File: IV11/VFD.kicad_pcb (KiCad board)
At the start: 2 copper layers, 225 x 80 mm, 72 parts, among them J1 USB_B, J2 I2C_CONN, SW1 switch, SW2 switch, SW3 switch, SW4 switch, U1 74HC595, U10 UDN2981, U11 UDN2981, U12 UDN2981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

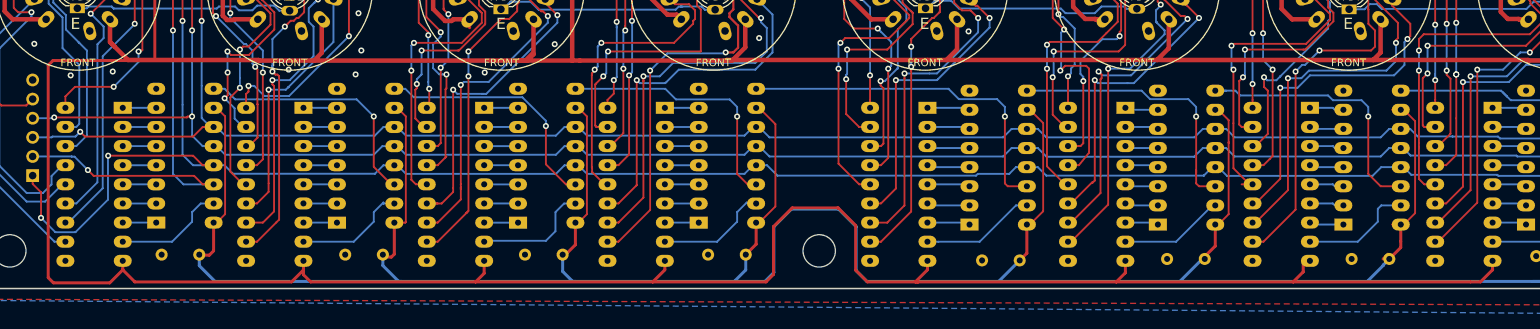
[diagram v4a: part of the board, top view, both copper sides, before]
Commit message: Update thickness of 48VDC tracks x
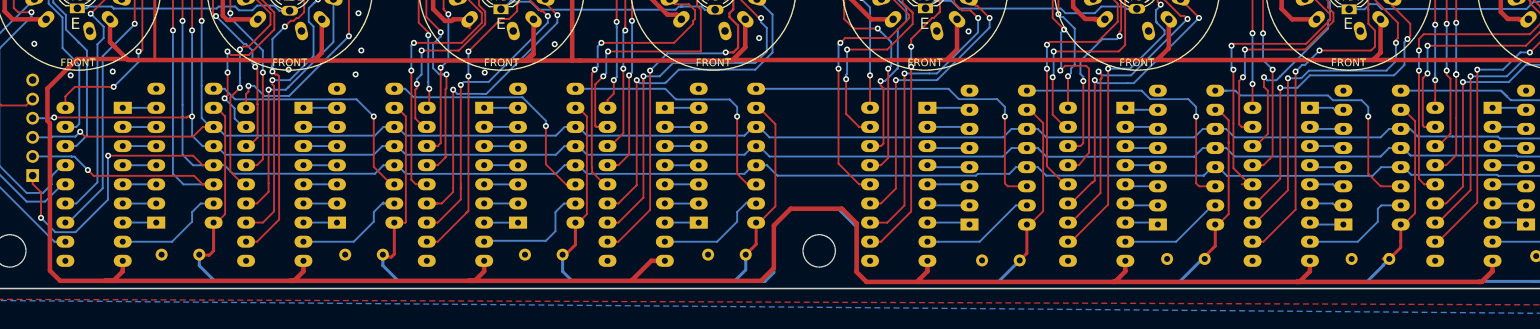
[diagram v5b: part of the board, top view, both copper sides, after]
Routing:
- net +36V: track 748.7 -> 803.5 mm
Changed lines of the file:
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@@
     (thickness 1.6)
     (drawings 15)
-    (tracks 2305)
+    (tracks 2318)
     (zones 0)
     (modules 72)
@@
   (segment (start 74.55514 44.242641) (end 74.55514 48.50786) (width 0.4) (layer F.Cu) (net 11))
   (segment (start 73.7235 49.7205) (end 73.3425 49.7205) (width 0.4) (layer F.Cu) (net 11))
-  (segment (start 10.7315 49.7205) (end 10.0965 50.3555) (width 0.4) (layer F.Cu) (net 11))
-  (segment (start 10.795 79.248) (end 18.272 79.248) (width 0.4) (layer F.Cu) (net 11))
-  (segment (start 10.0965 50.3555) (end 10.0965 78.5495) (width 0.4) (layer F.Cu) (net 11))
-  (segment (start 20 77.52) (end 20 76.32) (width 0.4) (layer F.Cu) (net 11))
-  (segment (start 10.0965 78.5495) (end 10.795 79.248) (width 0.4) (layer F.Cu) (net 11))
-  (segment (start 20.7645 49.7205) (end 10.7315 49.7205) (width 0.4) (layer F.Cu) (net 11))
-  (segment (start 18.272 79.248) (end 20 77.52) (width 0.4) (layer F.Cu) (net 11))
-  (segment (start 20 77.52) (end 21.601 79.121) (width 0.4) (layer F.Cu) (net 11))
-  (segment (start 21.601 79.121) (end 42.418 79.121) (width 0.4) (layer F.Cu) (net 11))
-  (segment (start 44 77.539) (end 44 76.32) (width 0.4) (layer F.Cu) (net 11))
-  (segment (start 42.418 79.121) (end 44 77.539) (width 0.4) (layer F.Cu) (net 11))
-  (segment (start 44 77.539) (end 44 78.163) (width 0.4) (layer F.Cu) (net 11))
-  (segment (start 44 78.163) (end 44.958 79.121) (width 0.4) (layer F.Cu) (net 11))
-  (segment (start 44.958 79.121) (end 66.8655 79.121) (width 0.4) (layer F.Cu) (net 11))
-  (segment (start 68 77.9865) (end 68 76.32) (width 0.4) (layer F.Cu) (net 11))
-  (segment (start 66.8655 79.121) (end 68 77.9865) (width 0.4) (layer F.Cu) (net 11))
-  (segment (start 90.399 79.121) (end 66.8655 79.121) (width 0.4) (layer F.Cu) (net 11))
-  (segment (start 92 77.52) (end 90.399 79.121) (width 0.4) (layer F.Cu) (net 11))
-  (segment (start 92 76.32) (end 92 77.52) (width 0.4) (layer F.Cu) (net 11))
-  (segment (start 126.873 77.52) (end 125.272 79.121) (width 0.4) (layer F.Cu) (net 11))
-  (segment (start 126.873 76.32) (end 126.873 77.52) (width 0.4) (layer F.Cu) (net 11))
-  (segment (start 153.162 77.9145) (end 153.162 76.32) (width 0.4) (layer F.Cu) (net 11))
-  (segment (start 151.9555 79.121) (end 153.162 77.9145) (width 0.4) (layer F.Cu) (net 11))
-  (segment (start 176.784 77.7875) (end 176.784 76.32) (width 0.4) (layer F.Cu) (net 11))
   (segment (start 151.9555 79.121) (end 175.4505 79.121) (width 0.4) (layer F.Cu) (net 11))
-  (segment (start 175.4505 79.121) (end 176.784 77.7875) (width 0.4) (layer F.Cu) (net 11))
   (segment (start 175.4505 79.121) (end 199.0025 79.121) (width 0.4) (layer F.Cu) (net 11))
   (segment (start 200.329 79.121) (end 199.0025 79.121) (width 0.4) (layer F.Cu) (net 11))
   (segment (start 201.93 77.52) (end 200.329 79.121) (width 0.4) (layer F.Cu) (net 11))
   (segment (start 201.93 76.32) (end 201.93 77.52) (width 0.4) (layer F.Cu) (net 11))
-  (segment (start 90.399 79.121) (end 105.4354 79.121) (width 0.4) (layer F.Cu) (net 11))
-  (segment (start 105.4354 79.121) (end 106.426 78.1304) (width 0.4) (layer F.Cu) (net 11))
-  (segment (start 106.426 78.1304) (end 106.426 71.7804) (width 0.4) (layer F.Cu) (net 11))
-  (segment (start 106.426 71.7804) (end 108.9152 69.2912) (width 0.4) (layer F.Cu) (net 11))
-  (segment (start 108.9152 69.2912) (end 115.0112 69.2912) (width 0.4) (layer F.Cu) (net 11))
-  (segment (start 115.0112 69.2912) (end 117.348 71.628) (width 0.4) (layer F.Cu) (net 11))
-  (segment (start 117.348 71.628) (end 117.348 77.5716) (width 0.4) (layer F.Cu) (net 11))
-  (segment (start 118.8974 79.121) (end 125.6284 79.121) (width 0.4) (layer F.Cu) (net 11))
-  (segment (start 117.348 77.5716) (end 118.8974 79.121) (width 0.4) (layer F.Cu) (net 11))
-  (segment (start 125.272 79.121) (end 125.6284 79.121) (width 0.4) (layer F.Cu) (net 11))
-  (segment (start 125.6284 79.121) (end 151.9555 79.121) (width 0.4) (layer F.Cu) (net 11))
   (segment (start 24.257 49.7205) (end 24.257 37.084) (width 0.4) (layer F.Cu) (net 11))
   (segment (start 24.257 49.7205) (end 20.7645 49.7205) (width 0.4) (layer F.Cu) (net 11))
@@
   (segment (start 18.30514 47.26114) (end 18.923 47.879) (width 0.6) (layer F.Cu) (net 11))
   (segment (start 18.30514 44.242641) (end 18.30514 47.26114) (width 0.6) (layer F.Cu) (net 11))
-  (segment (start 20.7645 49.7205) (end 18.923 47.879) (width 0.4) (layer F.Cu) (net 11))
   (segment (start 18.923 47.879) (end 18.542 47.498) (width 0.4) (layer F.Cu) (net 11))
   (segment (start 46.43014 48.69286) (end 45.4025 49.7205) (width 0.6) (layer F.Cu) (net 11))
@@
   (segment (start 79.756 31.75) (end 79.6925 31.6865) (width 0.6) (layer F.Cu) (net 11))
   (segment (start 80.772 31.75) (end 79.756 31.75) (width 0.6) (layer F.Cu) (net 11))
+  (segment (start 9.996499 57.709001) (end 9.996499 53.441499) (width 0.6) (layer F.Cu) (net 11))
+  (segment (start 11.675 78.975) (end 10.325 77.625) (width 0.6) (layer F.Cu) (net 11))
+  (segment (start 10.325 58.037502) (end 9.996499 57.709001) (width 0.6) (layer F.Cu) (net 11))
+  (segment (start 10.325 77.625) (end 10.325 58.037502) (width 0.6) (layer F.Cu) (net 11))
+  (segment (start 13.922498 49.5155) (end 12.768999 50.668999) (width 0.6) (layer F.Cu) (net 11))
+  (segment (start 20.5595 49.5155) (end 13.922498 49.5155) (width 0.6) (layer F.Cu) (net 11))
+  (segment (start 20.7645 49.7205) (end 20.5595 49.5155) (width 0.4) (layer F.Cu) (net 11))
+  (segment (start 20.5595 49.5155) (end 18.923 47.879) (width 0.4) (layer F.Cu) (net 11))
+  (segment (start 9.996499 53.441499) (end 12.768999 50.668999) (width 0.6) (layer F.Cu) (net 11))
+  (segment (start 18.745 78.975) (end 18.225 78.975) (width 0.6) (layer F.Cu) (net 11))
+  (segment (start 90.2 76.32) (end 87.545 78.975) (width 0.6) (layer F.Cu) (net 11))
+  (segment (start 92 76.32) (end 90.2 76.32) (width 0.6) (layer F.Cu) (net 11))
+  (segment (start 18.225 78.975) (end 17.675 78.975) (width 0.6) (layer F.Cu) (net 11))
+  (segment (start 17.675 78.975) (end 11.675 78.975) (width 0.6) (layer F.Cu) (net 11))
+  (segment (start 66.745 78.975) (end 65.925 78.975) (width 0.6) (layer F.Cu) (net 11))
+  (segment (start 68 77.72) (end 66.745 78.975) (width 0.6) (layer F.Cu) (net 11))
+  (segment (start 68 76.32) (end 68 77.72) (width 0.6) (layer F.Cu) (net 11))
+  (segment (start 87.545 78.975) (end 65.925 78.975) (width 0.6) (layer F.Cu) (net 11))
+  (segment (start 44 77.72) (end 42.745 78.975) (width 0.6) (layer F.Cu) (net 11))
+  (segment (start 44 76.32) (end 44 77.72) (width 0.6) (layer F.Cu) (net 11))
+  (segment (start 42.745 78.975) (end 42.25 78.975) (width 0.6) (layer F.Cu) (net 11))
+  (segment (start 65.925 78.975) (end 42.25 78.975) (width 0.6) (layer F.Cu) (net 11))
+  (segment (start 42.25 78.975) (end 17.675 78.975) (width 0.6) (layer F.Cu) (net 11))
+  (segment (start 20 77.72) (end 18.745 78.975) (width 0.6) (layer F.Cu) (net 11))
+  (segment (start 20 76.32) (end 20 77.72) (width 0.6) (layer F.Cu) (net 11))
+  (segment (start 87.545 78.975) (end 104.775 78.975) (width 0.6) (layer F.Cu) (net 11))
+  (segment (start 104.775 78.975) (end 106.475 77.275) (width 0.6) (layer F.Cu) (net 11))
+  (segment (start 106.475 77.275) (end 106.475 71.625) (width 0.6) (layer F.Cu) (net 11))
+  (segment (start 106.475 71.625) (end 108.7 69.4) (width 0.6) (layer F.Cu) (net 11))
+  (segment (start 115.525 69.4) (end 117.475 71.35) (width 0.6) (layer F.Cu) (net 11))
+  (segment (start 108.7 69.4) (end 115.525 69.4) (width 0.6) (layer F.Cu) (net 11))
+  (segment (start 117.475 71.35) (end 117.475 77.825) (width 0.6) (layer F.Cu) (net 11))
+  (segment (start 117.475 77.825) (end 118.771 79.121) (width 0.6) (layer F.Cu) (net 11))
+  (segment (start 200.529 79.121) (end 200.079 79.121) (width 0.6) (layer F.Cu) (net 11))
+  (segment (start 201.93 76.32) (end 201.93 77.72) (width 0.6) (layer F.Cu) (net 11))
+  (segment (start 201.93 77.72) (end 200.529 79.121) (width 0.6) (layer F.Cu) (net 11))
+  (segment (start 200.079 79.121) (end 200.329 79.121) (width 0.6) (layer F.Cu) (net 11))
+  (segment (start 176.272 79.121) (end 175.896 79.121) (width 0.6) (layer F.Cu) (net 11))
+  (segment (start 177.673 77.72) (end 176.272 79.121) (width 0.6) (layer F.Cu) (net 11))
+  (segment (start 177.673 76.32) (end 177.673 77.72) (width 0.6) (layer F.Cu) (net 11))
+  (segment (start 175.896 79.121) (end 200.079 79.121) (width 0.6) (layer F.Cu) (net 11))
+  (segment (start 151.761 79.121) (end 151.529 79.121) (width 0.6) (layer F.Cu) (net 11))
+  (segment (start 153.162 77.72) (end 151.761 79.121) (width 0.6) (layer F.Cu) (net 11))
+  (segment (start 153.162 76.32) (end 153.162 77.72) (width 0.6) (layer F.Cu) (net 11))
+  (segment (start 151.529 79.121) (end 175.896 79.121) (width 0.6) (layer F.Cu) (net 11))
+  (segment (start 125.729 78.864) (end 125.729 79.121) (width 0.6) (layer F.Cu) (net 11))
+  (segment (start 126.873 77.72) (end 125.729 78.864) (width 0.6) (layer F.Cu) (net 11))
+  (segment (start 126.873 76.32) (end 126.873 77.72) (width 0.6) (layer F.Cu) (net 11))
+  (segment (start 118.771 79.121) (end 125.729 79.121) (width 0.6) (layer F.Cu) (net 11))
+  (segment (start 125.729 79.121) (end 151.529 79.121) (width 0.6) (layer F.Cu) (net 11))
   (segment (start 66.069859 44.24264) (end 66.069859 45.365015) (width 0.4) (layer F.Cu) (net 12))
   (segment (start 9.006 28.7765) (end 8.9645 28.7765) (width 0.4) (layer F.Cu) (net 12))
